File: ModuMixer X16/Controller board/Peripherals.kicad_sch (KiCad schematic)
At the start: 37 parts, among them J1 Conn_01x03_Pin, J2 Conn_02x04_Counter_Clockwise, J3 Conn_02x07_Counter_Clockwise, J4 Conn_01x05_Pin, J5 Conn_02x07_Counter_Clockwise, J8 Conn_02x25_Counter_Clockwise, J9 Conn_02x25_Counter_Clockwise, Q1 MMBT2222A, SW1 Enter, SW10 SW_Push, SW11 SW_Push, SW12 SW_Push, SW13 SW_Push, SW14 SW_Push, SW15 SW_Push, SW16 SW_Push, SW17 SW_Push, SW18 SW_Push, SW19 SW_Push, SW2 Up, SW20 RotaryEncoder_Switch_MP, SW21 RotaryEncoder_Switch_MP, SW22 RotaryEncoder_Switch_MP, SW23 RotaryEncoder_Switch_MP, SW24 RotaryEncoder_Switch_MP, SW25 RotaryEncoder_Switch_MP, SW3 Down, SW4 Left, SW5 RotaryEncoder_Switch_MP, SW6 RotaryEncoder_Switch_MP, SW7 RotaryEncoder_Switch_MP, SW8 Right, SW9 SW_Push

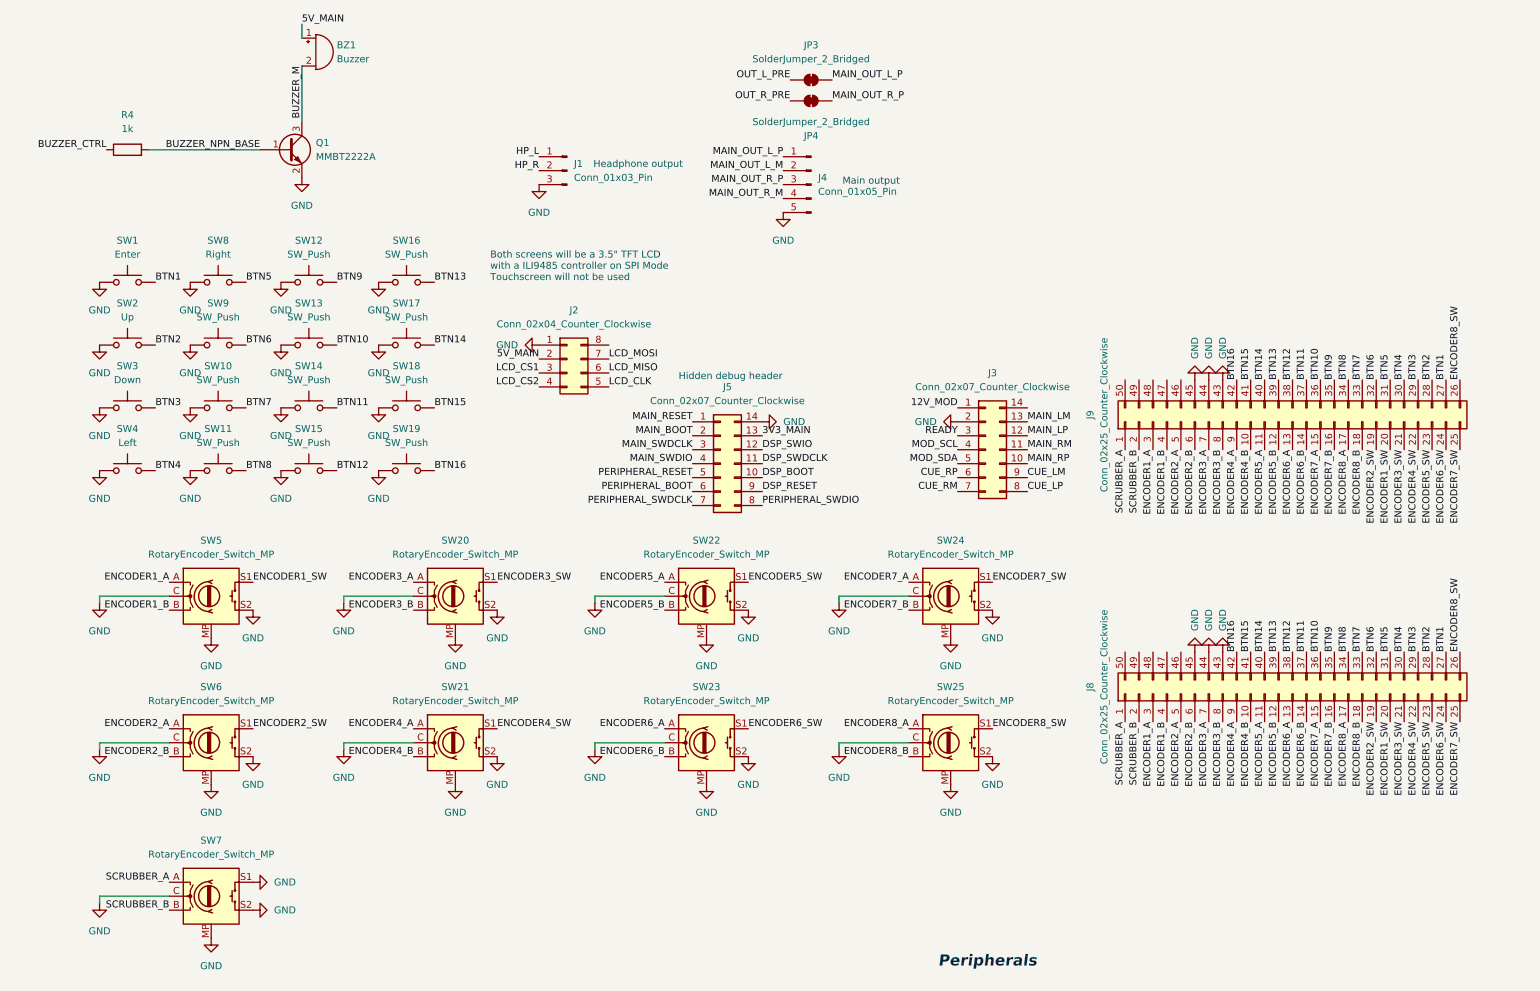
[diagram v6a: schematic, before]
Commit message: Changed all labels to global
I made it in a rather hacky way (editing all files on notepad with Ctrl + H), i'm only reverting this if something breaks
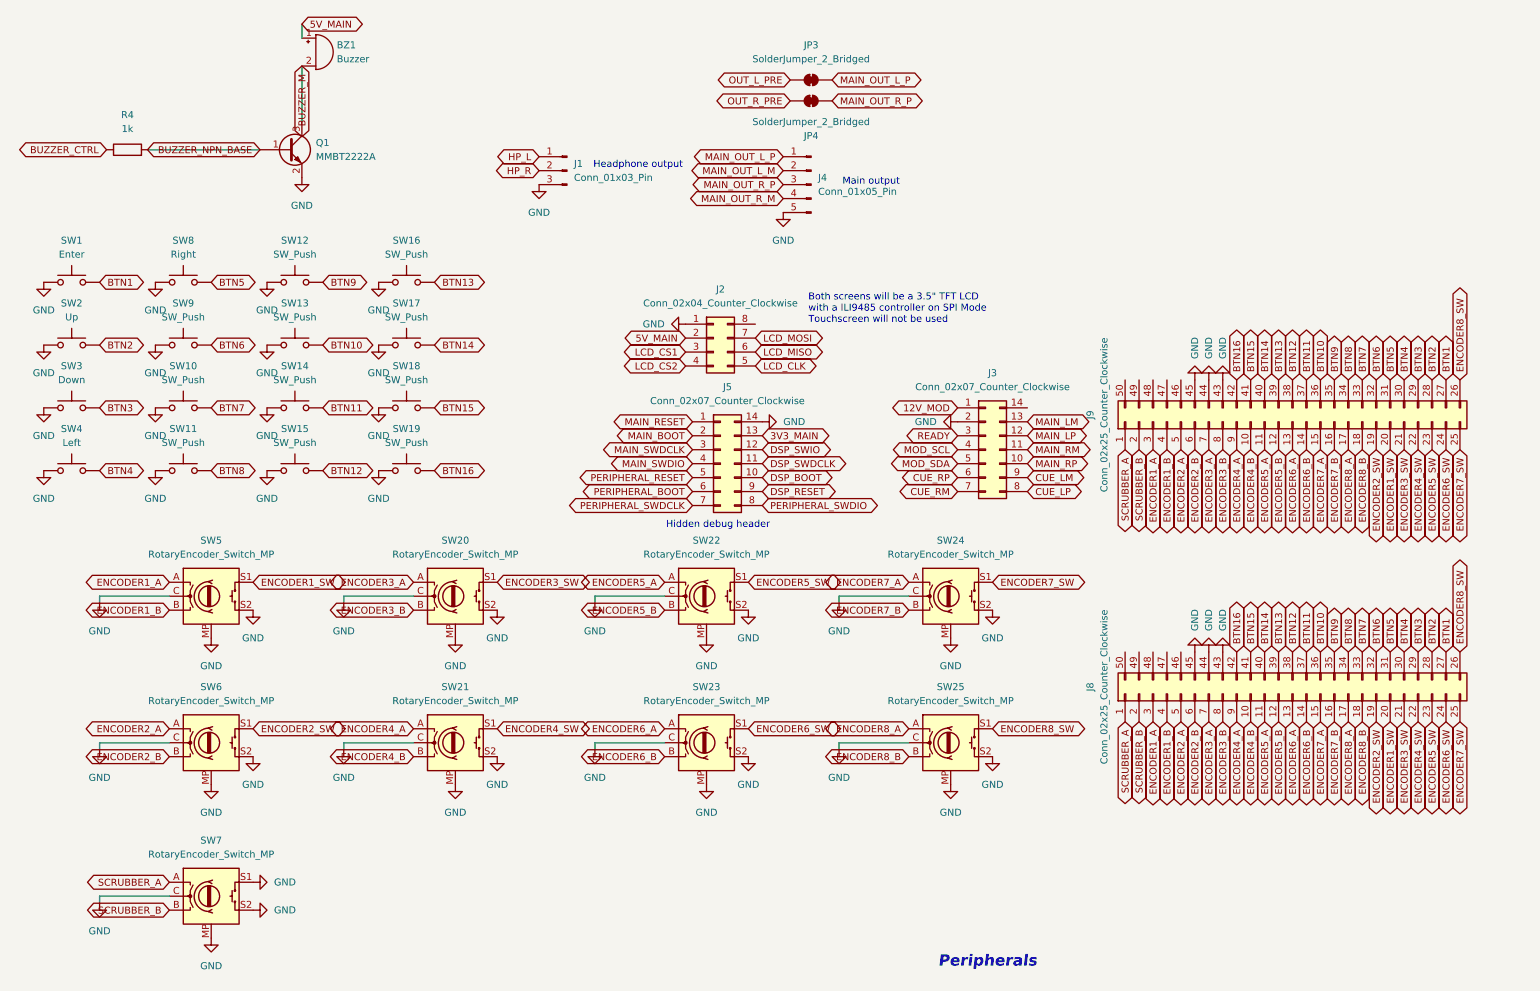
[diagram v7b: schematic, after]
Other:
- moved on the sheet: J2, SW1, SW10, SW11, SW12, SW13, SW14, SW15, SW2, SW3, SW4, SW8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
